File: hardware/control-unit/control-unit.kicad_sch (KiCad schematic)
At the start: 23 parts

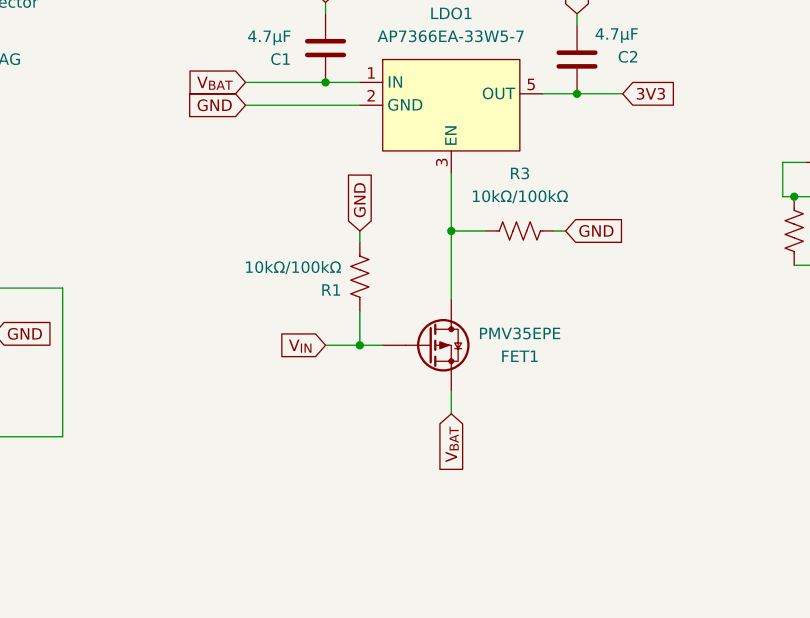
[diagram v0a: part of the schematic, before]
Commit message: Replaced P-channel FET at LDO EN pin with N-channel
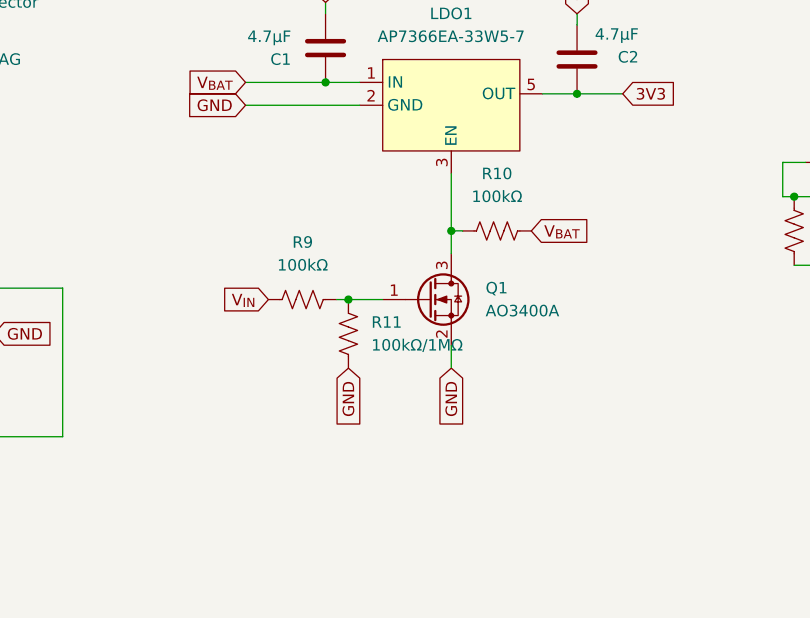
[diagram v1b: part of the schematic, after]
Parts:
- removed FET1: PMV35EPE, Package_TO_SOT_SMD:SOT-23_Handsoldering, symbol Custom_Symbols:PMV35EPE
- removed R1, R3: 10kΩ/100kΩ, Resistor_SMD:R_0805_2012Metric_Pad1.20x1.40mm_HandSolder, symbol Device:R_US
- added Q1: AO3400A, Package_TO_SOT_SMD:SOT-23, symbol Transistor_FET:AO3400A
- added R10, R9: 100kΩ, Resistor_SMD:R_0805_2012Metric_Pad1.20x1.40mm_HandSolder, symbol Device:R_US
- added R11: 100kΩ/1MΩ, Resistor_SMD:R_0805_2012Metric_Pad1.20x1.40mm_HandSolder, symbol Device:R_US
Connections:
- net GND: now also Q1.2 (S), R11.1
- net V_{BAT}: now also R10.2
- net V_{IN}: now also R9.1
- net at LDO1.3 (EN): now also Q1.3 (D), R10.1
- new net: Q1.1 (G), R11.2, R9.2
